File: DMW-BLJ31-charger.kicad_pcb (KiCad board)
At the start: 2 copper layers, 142.5 x 127.5 mm, 44 parts, among them J21 BAT-, J22 BAT-, J23 -, J24 BAT-, J25 BAT+, J26 +, J27 BAT+, J28 BAT+, J29 Vin, J30 Vin, J35 gnd, J36 gnd, J37 gnd, J42 BAT+, J43 BAT+, J44 +, J45 BAT+, J46 -, J47 gnd, J48 BAT-

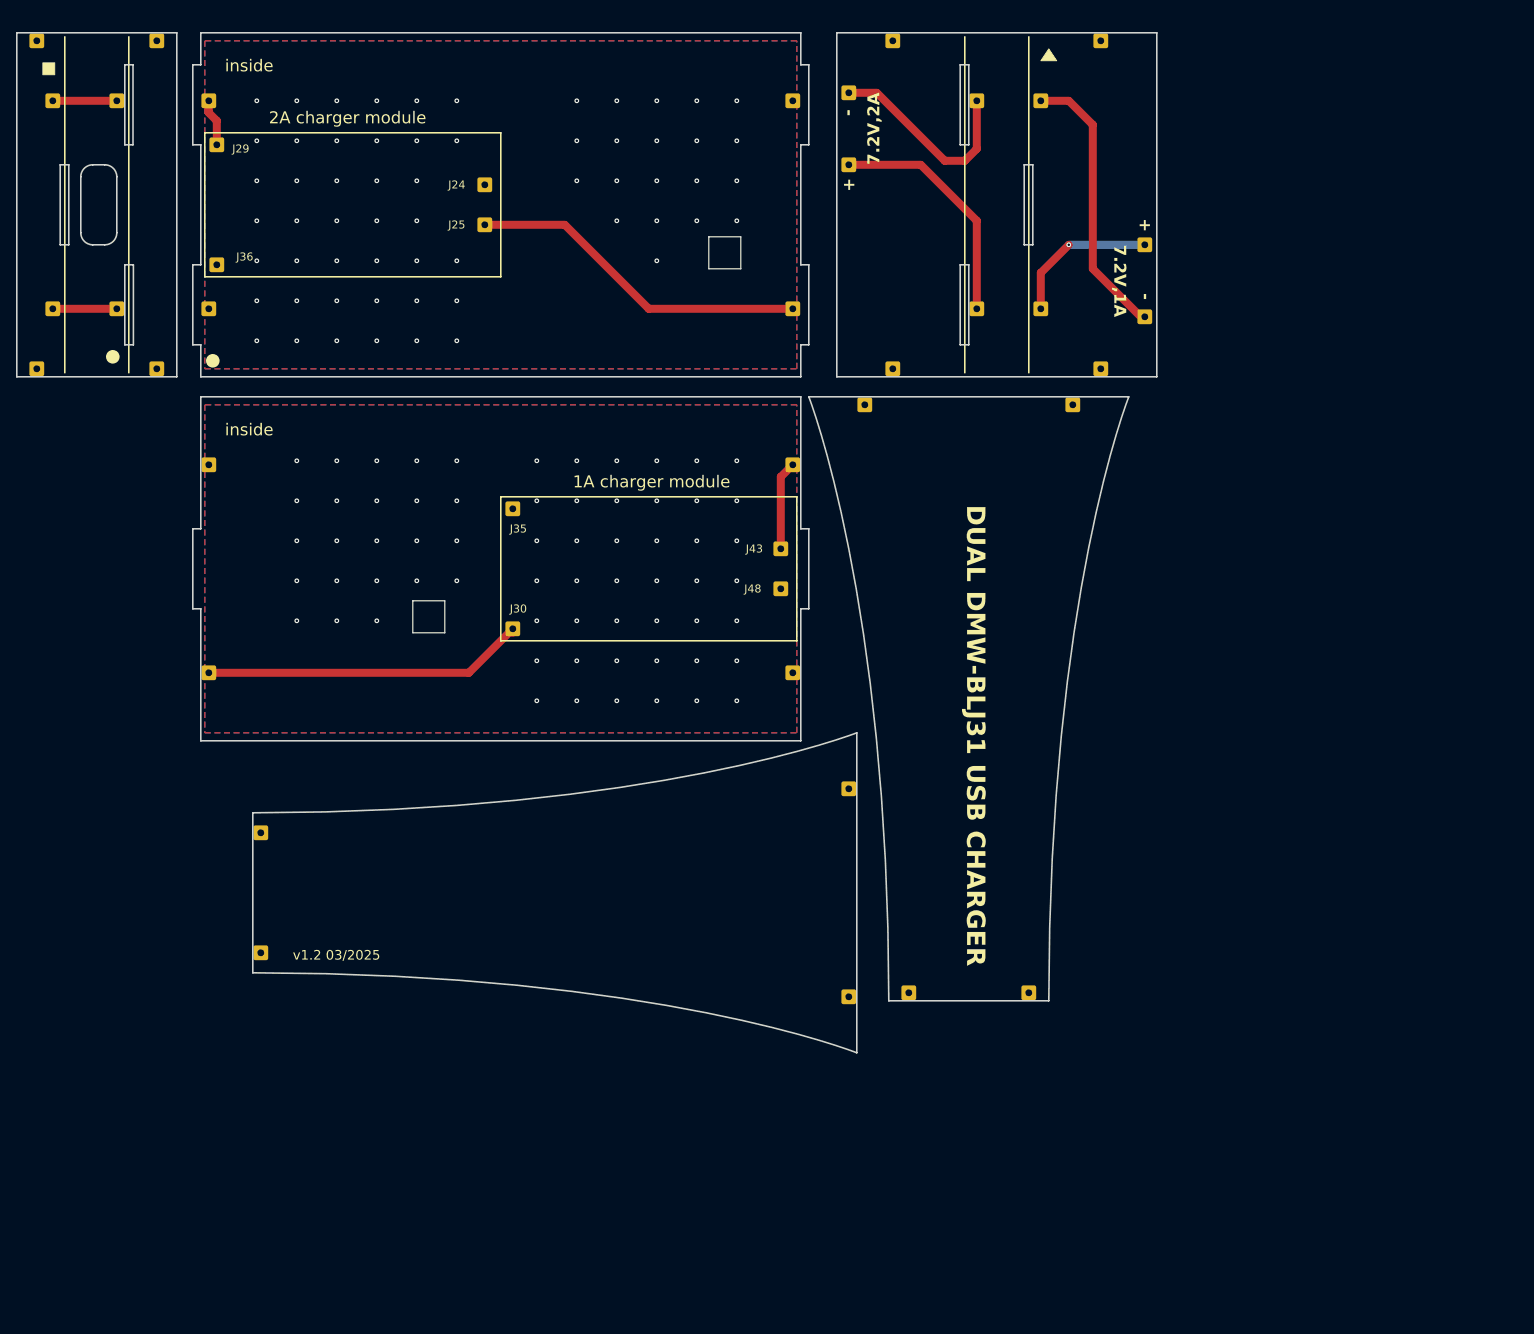
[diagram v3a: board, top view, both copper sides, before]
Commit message: redesign layout to minimize fabrication costs
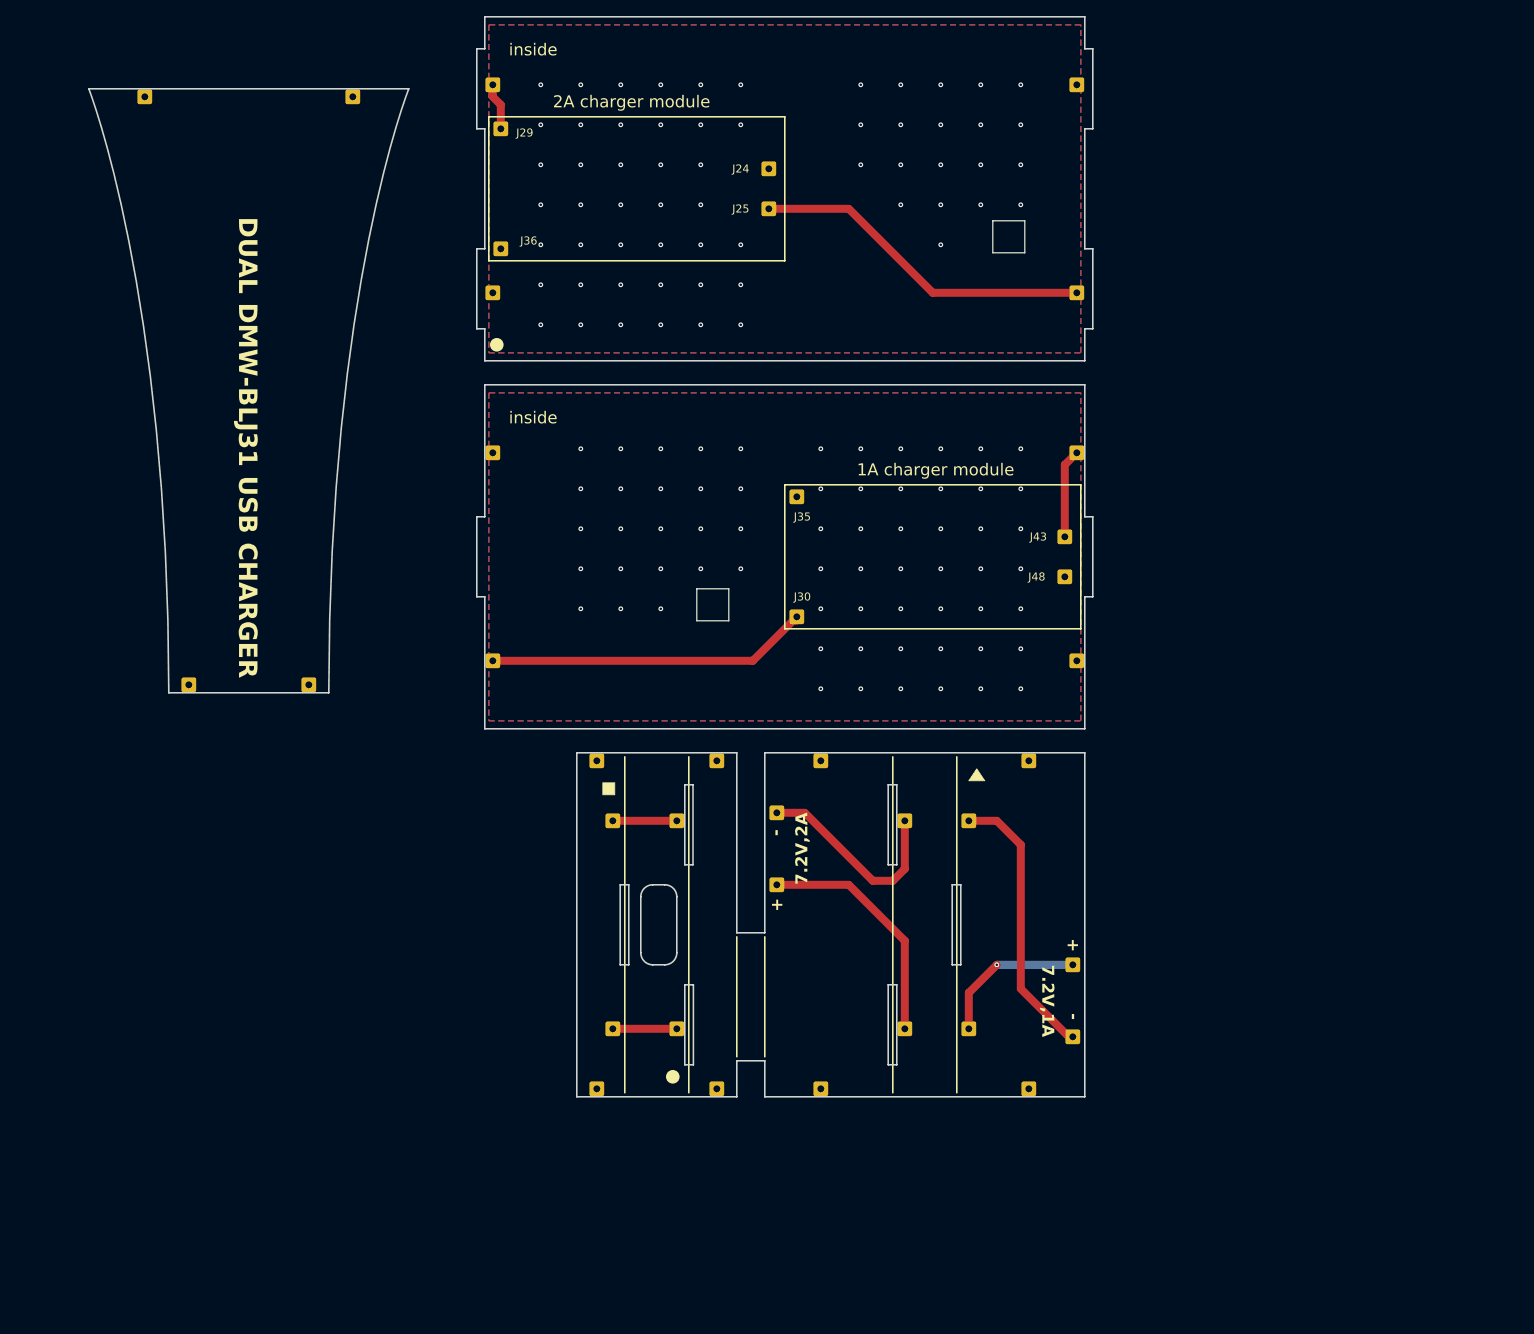
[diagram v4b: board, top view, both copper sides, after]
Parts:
- removed J19, J20, J5, J6: ~, Connector_Wire:SolderWire-0.25sqmm_1x01_D0.65mm_OD1.7mm
- added REF**: OSHW-Symbol_6.7x6mm_SilkScreen, Symbol:OSHW-Symbol_6.7x6mm_SilkScreen, B.Cu at (152.5, 123.5)
- added REF**: WEEE-Logo_4.2x6mm_SilkScreen, Symbol:WEEE-Logo_4.2x6mm_SilkScreen, B.Cu at (155.0, 155.2)
- moved J15 114.0 mm to (97.5, 158.5)
- moved J16 114.0 mm to (112.5, 158.5)
- moved J17 114.0 mm to (97.5, 117.5)
- moved J18 114.0 mm to (112.5, 117.5)
- moved J31 114.0 mm to (99.5, 125.0)
- moved J33 114.0 mm to (107.5, 125.0)
- moved J38 114.0 mm to (107.5, 151.0)
- moved J40 114.0 mm to (99.5, 151.0)
- moved J11 97.9 mm to (67.0, 34.5)
- moved J7 97.9 mm to (61.5, 108.0)
- moved J8 97.9 mm to (46.5, 108.0)
- moved J9 97.9 mm to (41.0, 34.5)
- moved J10 90.4 mm to (151.5, 117.5)
- moved J12 90.4 mm to (125.5, 117.5)
- moved J13 90.4 mm to (151.5, 158.5)
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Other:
- board size 142.5 x 127.5 mm -> 125.5 x 135 mm
- board text added: "v1.3 03/2025"
- board text removed: "v1.2 03/2025"

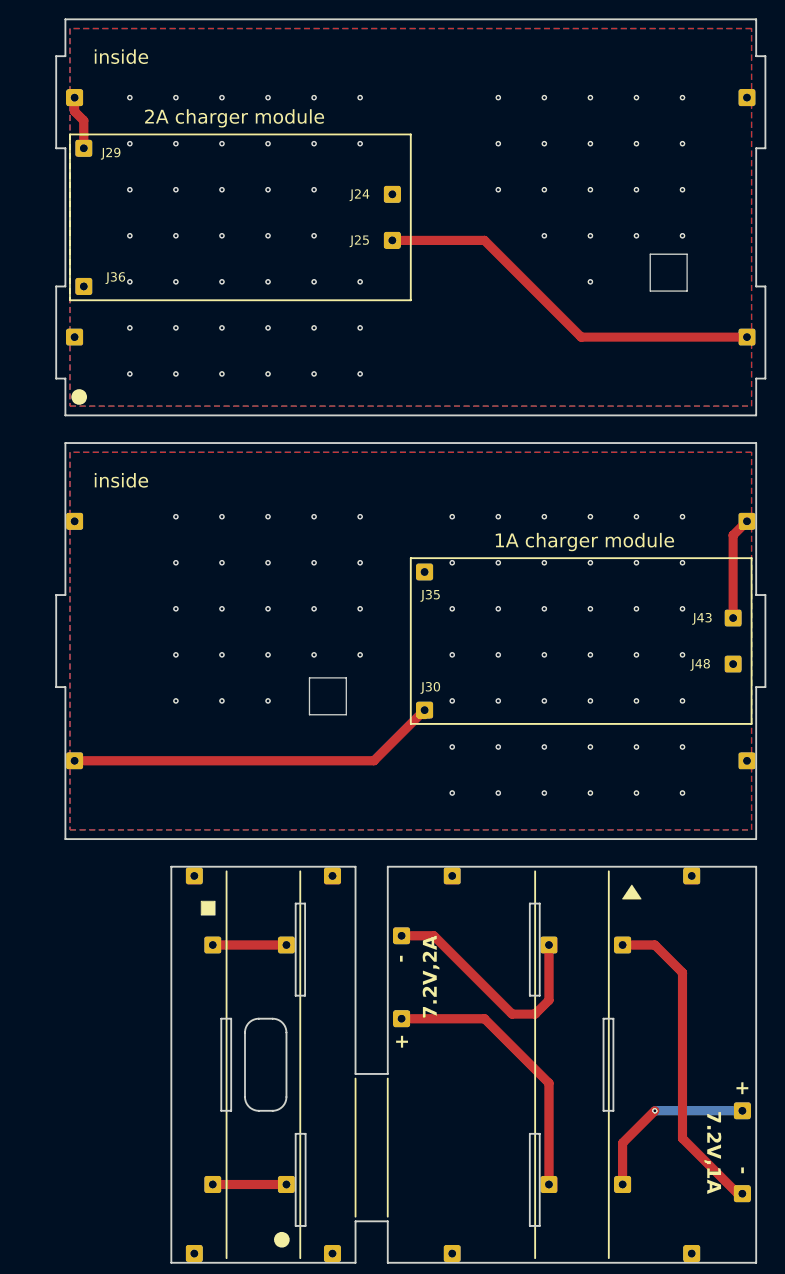
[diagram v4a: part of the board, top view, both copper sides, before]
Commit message: change vias
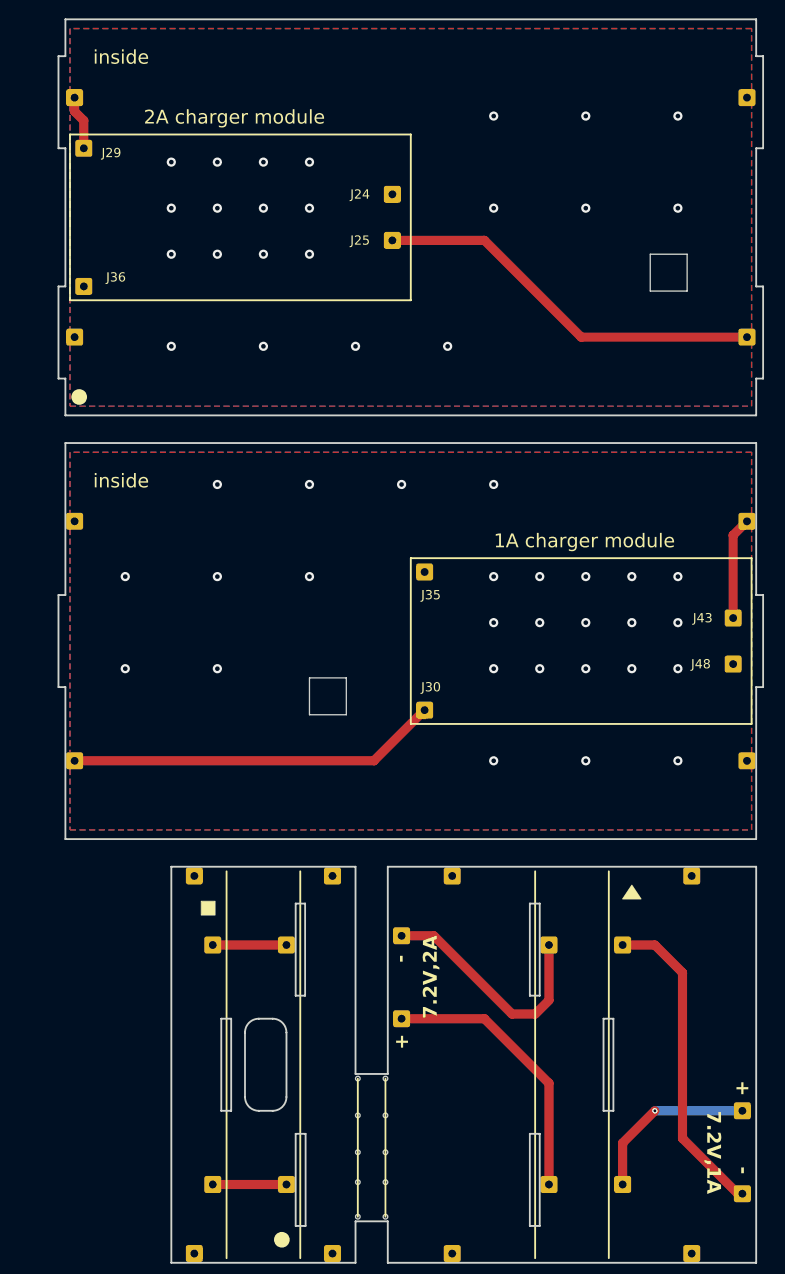
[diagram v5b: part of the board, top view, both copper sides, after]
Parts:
- added ?: , , F.Cu at (115.2, 150.8)
- added ?: , , F.Cu at (115.2, 139.5)
- added ?: , , F.Cu at (115.2, 143.5)
- added ?: , , F.Cu at (118.2, 154.5)
- added ?: , , F.Cu at (115.2, 147.5)
- added ?: , , F.Cu at (118.2, 143.5)
- added ?: , , F.Cu at (118.2, 150.8)
- added ?: , , F.Cu at (118.2, 139.5)
- added ?: , , F.Cu at (115.2, 154.5)
- added ?: , , F.Cu at (118.2, 147.5)
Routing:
- net GND: vias 125 -> 49
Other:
- board size 125.5 x 135 mm -> 125.2 x 135 mm
